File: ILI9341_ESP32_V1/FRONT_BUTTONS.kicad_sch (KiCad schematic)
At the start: 12 parts, among them J5 Micro_SD_Card_CD, SW10 SW_Push, SW11 SW_Push, SW12 SW_Push, SW2 SW_Push, SW3 SW_Push, SW4 SW_Push, SW5 SW_Push, SW9 SW_Push, U8 IPCB05501F20S3V, U9 IPCB05501M20S3V

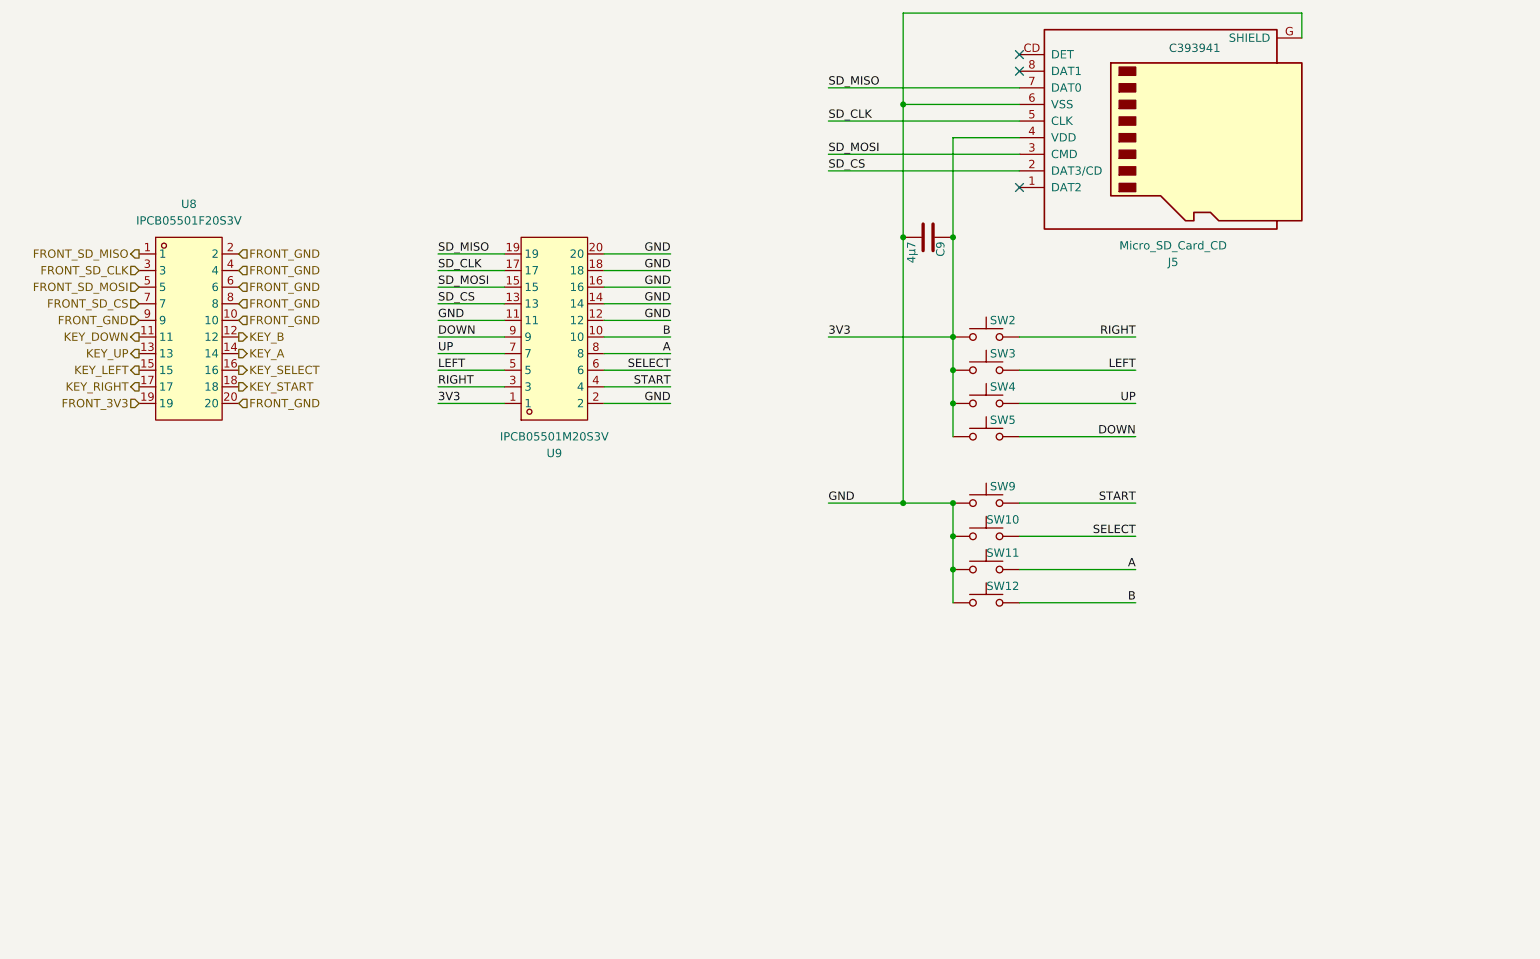
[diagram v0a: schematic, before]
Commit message: Update ESP from S3 to WROVER
Changed ESP to be compatible to odroid-go
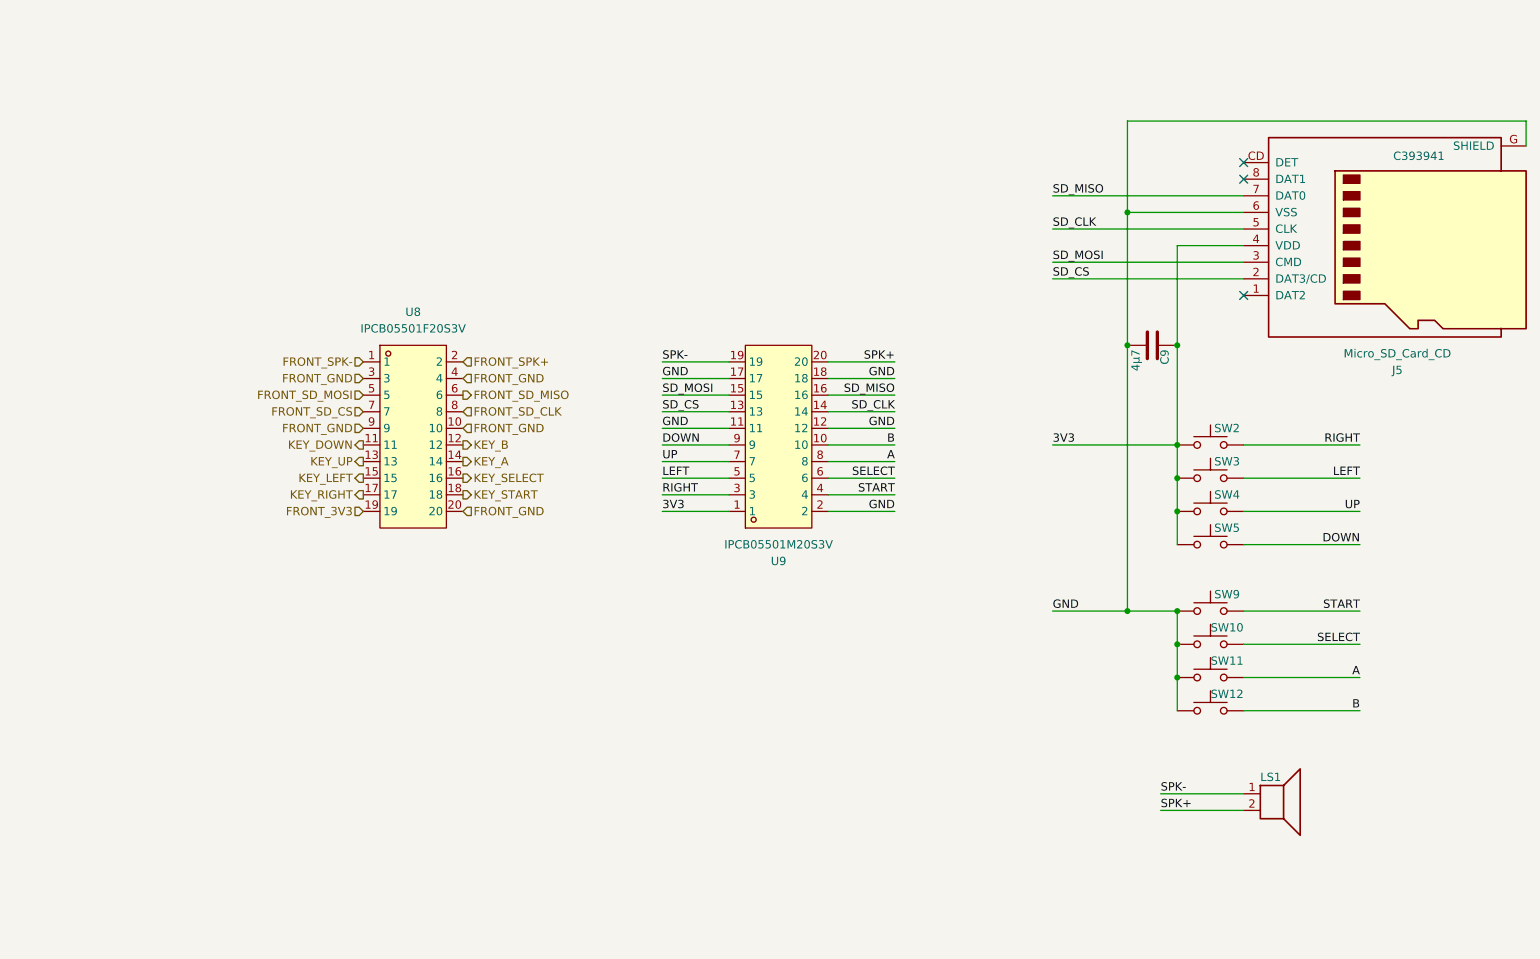
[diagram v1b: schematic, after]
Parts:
- added LS1: Speaker, Connector_PinHeader_2.54mm:PinHeader_1x02_P2.54mm_Vertical, symbol Device:Speaker
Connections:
- net FRONT_GND: now also U8.3; no longer U8.2, U8.6, U8.8
- net FRONT_SD_CLK: now also U8.8; no longer U8.3
- net FRONT_SD_MISO: now also U8.6; no longer U8.1
- net GND: now also U9.17; no longer U9.14, U9.16, U9.20
- net SD_CLK: now also U9.14; no longer U9.17
- net SD_MISO: now also U9.16; no longer U9.19
- new net FRONT_SPK+: U8.2
- new net FRONT_SPK-: U8.1
- new net SPK+: LS1.2, U9.20
- new net SPK-: LS1.1, U9.19
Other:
- moved on the sheet: C9, J5, SW10, SW11, SW12, SW2, SW3, SW4, SW5, SW9, U8, U9

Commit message: update cardridge grabber funktion
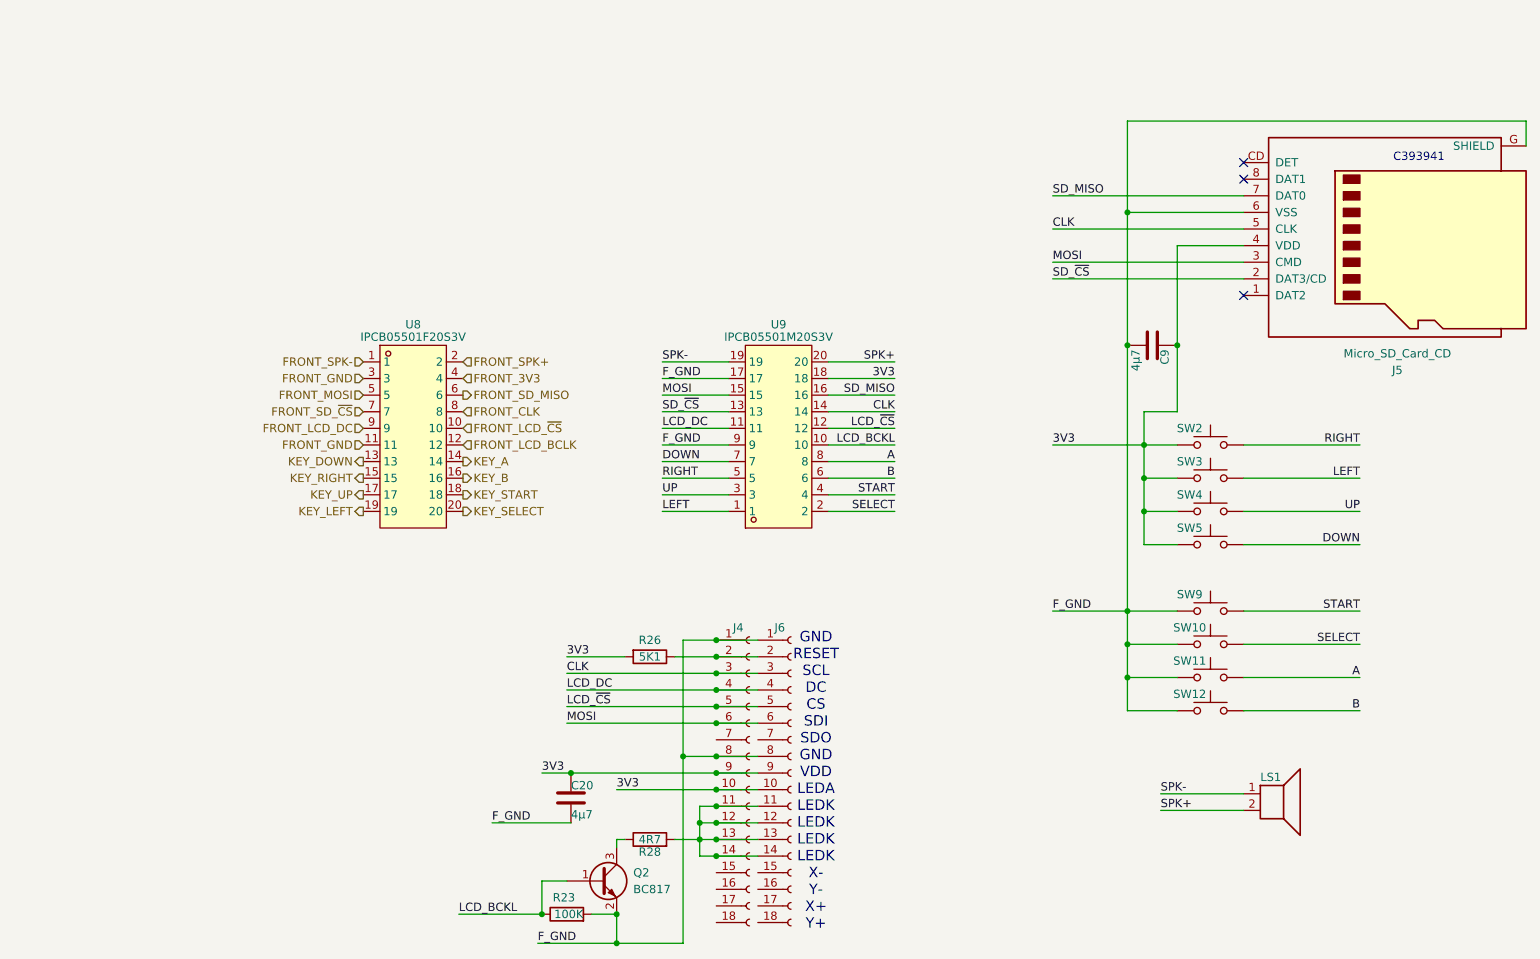
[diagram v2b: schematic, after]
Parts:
- added C20: 4µ7, Capacitor_SMD:C_1206_3216Metric, symbol Device:C
- added J4, J6: Conn_01x18_Socket, TheBrutzlers_Lib:solder connector 0.8mm 18 pin, symbol Connector:Conn_01x18_Socket
- added Q2: BC817, Package_TO_SOT_SMD:SOT-323_SC-70, symbol Transistor_BJT:BC817
- added R23: 100K, Resistor_SMD:R_0603_1608Metric_Pad0.98x0.95mm_HandSolder, symbol Device:R
- added R26: 5K1, Resistor_SMD:R_0603_1608Metric_Pad0.98x0.95mm_HandSolder, symbol Device:R
- added R28: 4R7, Resistor_SMD:R_0603_1608Metric_Pad0.98x0.95mm_HandSolder, symbol Device:R
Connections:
- net 3V3: now also U9.18, C20.1, J4.10 (Pin_10), J4.9 (Pin_9), J6.10 (Pin_10), J6.9 (Pin_9), R26.2; no longer U9.1
- net B: now also U9.6; no longer U9.10
- net DOWN: now also U9.7; no longer U9.9
- net FRONT_3V3: now also U8.4; no longer U8.19
- net FRONT_GND: now also U8.11; no longer U8.10, U8.20, U8.4, U8.9
- net KEY_B: now also U8.16; no longer U8.12
- net KEY_DOWN: now also U8.13; no longer U8.11
- net KEY_LEFT: now also U8.19; no longer U8.15
- net KEY_RIGHT: now also U8.15; no longer U8.17
- net KEY_SELECT: now also U8.20; no longer U8.16
- net KEY_UP: now also U8.17; no longer U8.13
- net LEFT: now also U9.1; no longer U9.5
- net RIGHT: now also U9.5; no longer U9.3
- net SELECT: now also U9.2; no longer U9.6
- net UP: now also U9.3; no longer U9.7
- net FRONT_SD_CLK renamed FRONT_CLK
- net FRONT_SD_CS renamed FRONT_SD_~{CS}
- net FRONT_SD_MOSI renamed FRONT_MOSI
- net GND renamed F_GND
- net F_GND: now also U9.9, C20.2, J4.1 (Pin_1), J4.8 (Pin_8), J6.1 (Pin_1), J6.8 (Pin_8), Q2.2 (E), R23.2; no longer U9.11, U9.12, U9.18, U9.2
- net SD_CLK renamed CLK
- net CLK: now also J4.3 (Pin_3), J6.3 (Pin_3)
- net SD_CS renamed SD_~{CS}
- net SD_MOSI renamed MOSI
- net MOSI: now also J4.6 (Pin_6), J6.6 (Pin_6)
- new net: Q2.3 (C), R28.1
- new net: J4.11 (Pin_11), J4.12 (Pin_12), J4.13 (Pin_13), J4.14 (Pin_14), J6.11 (Pin_11), J6.12 (Pin_12), J6.13 (Pin_13), J6.14 (Pin_14), R28.2
- new net: J4.2 (Pin_2), J6.2 (Pin_2), R26.1
- new net FRONT_LCD_BCLK: U8.12
- new net FRONT_LCD_DC: U8.9
- new net FRONT_LCD_~{CS}: U8.10
- new net LCD_BCKL: Q2.1 (B), R23.1, U9.10
- new net LCD_DC: J4.4 (Pin_4), J6.4 (Pin_4), U9.11
- new net LCD_~{CS}: J4.5 (Pin_5), J6.5 (Pin_5), U9.12
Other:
- note added: "GND RESET SCL DC CS SDI SDO GND VDD LEDA LEDK LEDK LEDK LEDK X- Y- X+ Y+"

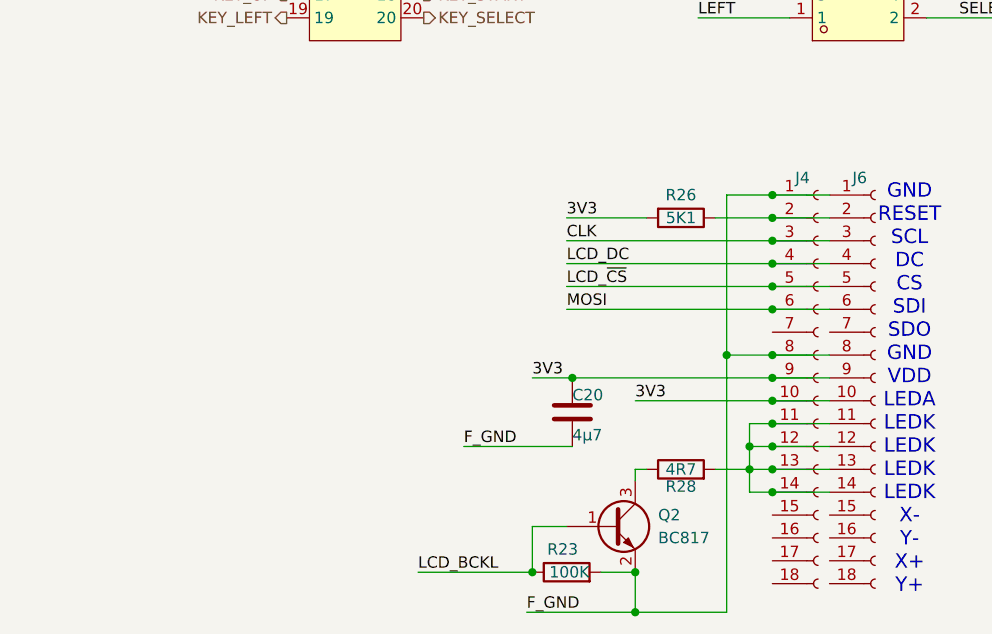
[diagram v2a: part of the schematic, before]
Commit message: update routing and put display on front pcb
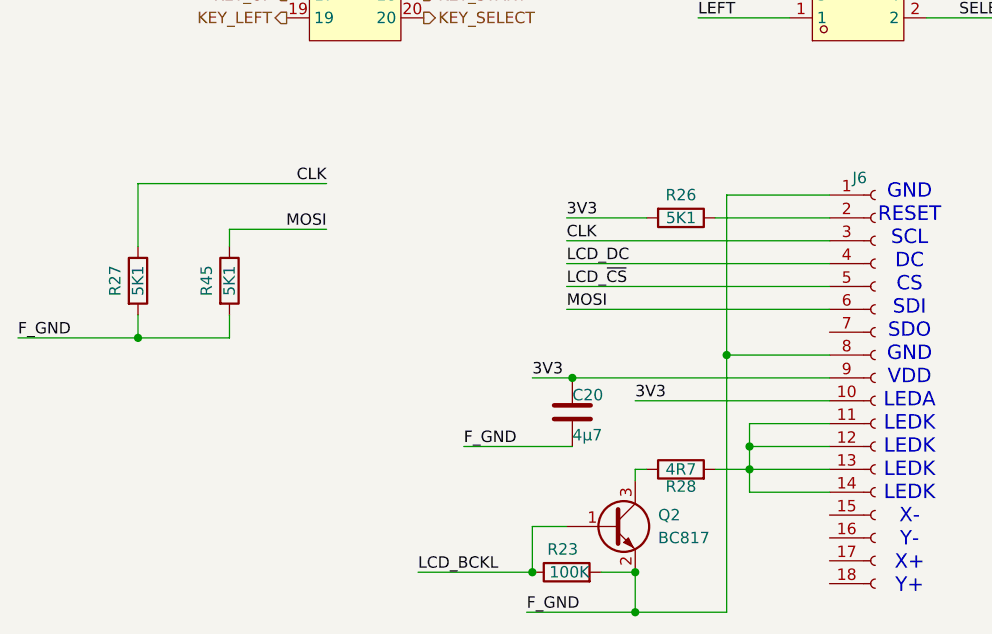
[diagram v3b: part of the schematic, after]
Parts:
- removed J4: Conn_01x18_Socket, TheBrutzlers_Lib:solder connector 0.8mm 18 pin, symbol Connector:Conn_01x18_Socket
- added R27, R45: 5K1, Resistor_SMD:R_0603_1608Metric_Pad0.98x0.95mm_HandSolder, symbol Device:R
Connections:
- net CLK: now also R27.1
- net F_GND: now also R27.2, R45.2
- net MOSI: now also R45.1
